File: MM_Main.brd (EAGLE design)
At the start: 74 x 87.2 mm, 81 parts, among them IC1 ULN2003AD, IC2 TB6612FNG, IC4 LD117ADT50TR, IC5 MCP1825, Q1 TEFT4300, Q2 TEFT4300, Q3 TEFT4300, Q4 TEFT4300, Q5 TEFT4300, Q6 TEFT4300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

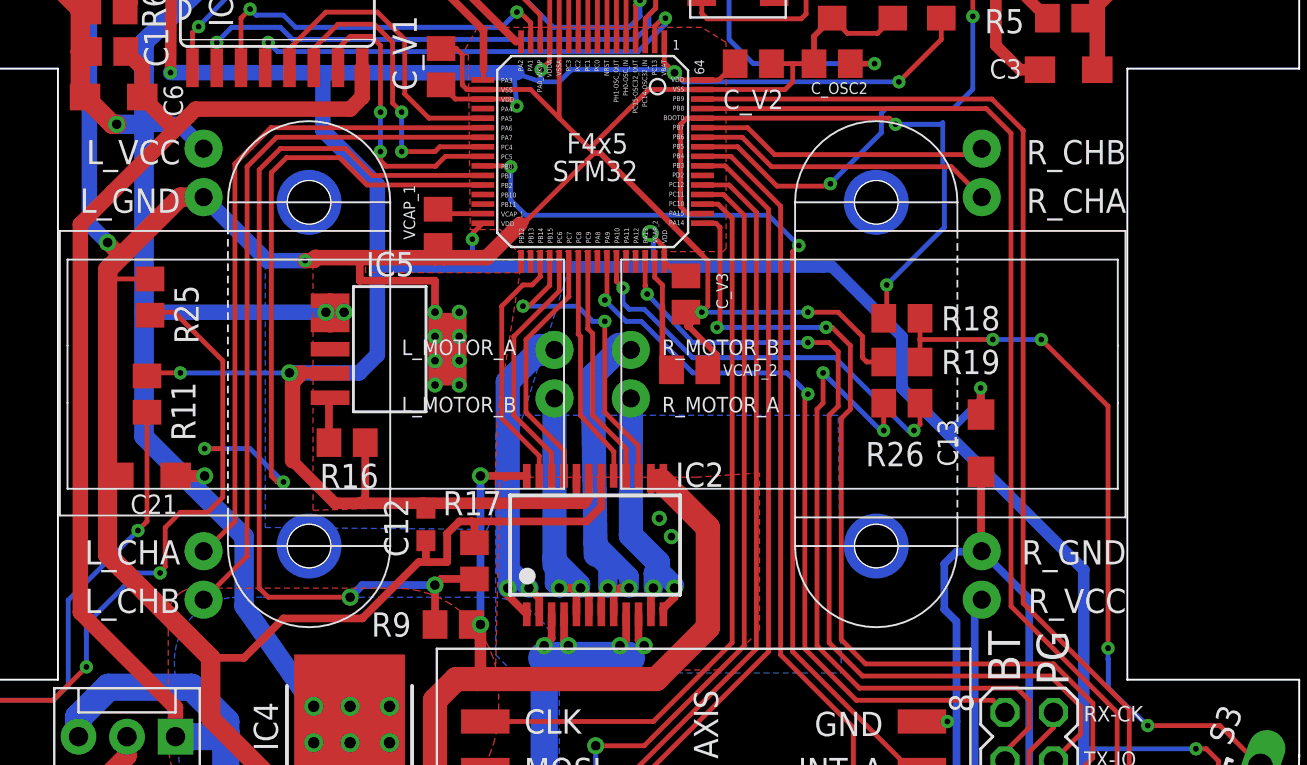
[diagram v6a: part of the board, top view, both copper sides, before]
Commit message: wywalilem elementy ktore byly pod podstawka silnika
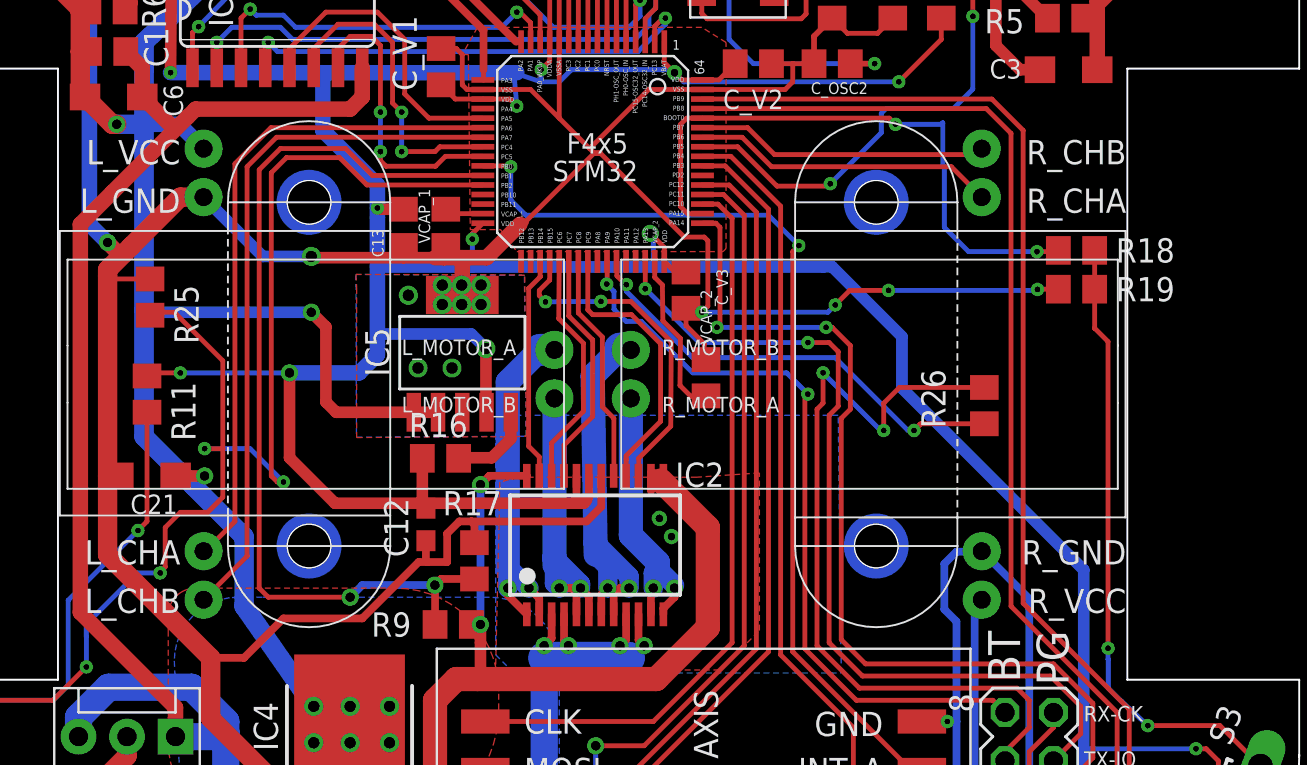
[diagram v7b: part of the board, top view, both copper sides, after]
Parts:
- C13: value tant-a-10u -> 10u; device rcl:SMC_A -> rcl:C0805
- moved C13 32.3 mm to (-9.91, 7.62)
- moved R19 9.91 mm to (25.3, 4.38)
- moved R18 9.81 mm to (25.3, 6.41)
- moved R16 4.96 mm to (-7.97, -4.48), turned to 180 degrees
- moved R26 4.32 mm to (20.5, -1.71), turned to 270 degrees
- moved IC5 3.46 mm to (-6.92, 1.30), turned to 0 degrees
- moved VCAP_2 0.95 mm to (5.94, -0.25), turned to 90 degrees
- moved VCAP_1 0.41 mm to (-7.69, 7.62)
- moved C_V3 0.20 mm to (4.89, 4.33)
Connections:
- net +3V3: now also C13.1; no longer C13.+
- net GND: now also C13.2; no longer C13.-
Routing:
- net +5V: track 298.1 -> 305.8 mm, vias 16 -> 15
- net GND: track 466.4 -> 459.1 mm, vias 20 -> 23
- net N$26: track 36.3 -> 41.9 mm
- net N$23: track 38.0 -> 32.8 mm, vias 4 -> 2
- net +3V3: track 351.2 -> 355.7 mm, vias 14 -> 15
- net MR_IN2: track 12.1 -> 14.7 mm
- net VCAP_2: track 6.32 -> 8.65 mm
- net BT_TXD: track 21.9 -> 24.2 mm
- net N$1: track 2.38 -> 4.54 mm
- net ML_PWM: track 13.2 -> 11.7 mm
- net MR_PWM: track 16.6 -> 17.7 mm
- net ML_IN2: track 13.0 -> 12.4 mm
- net ML_IN1: track 13.0 -> 12.5 mm

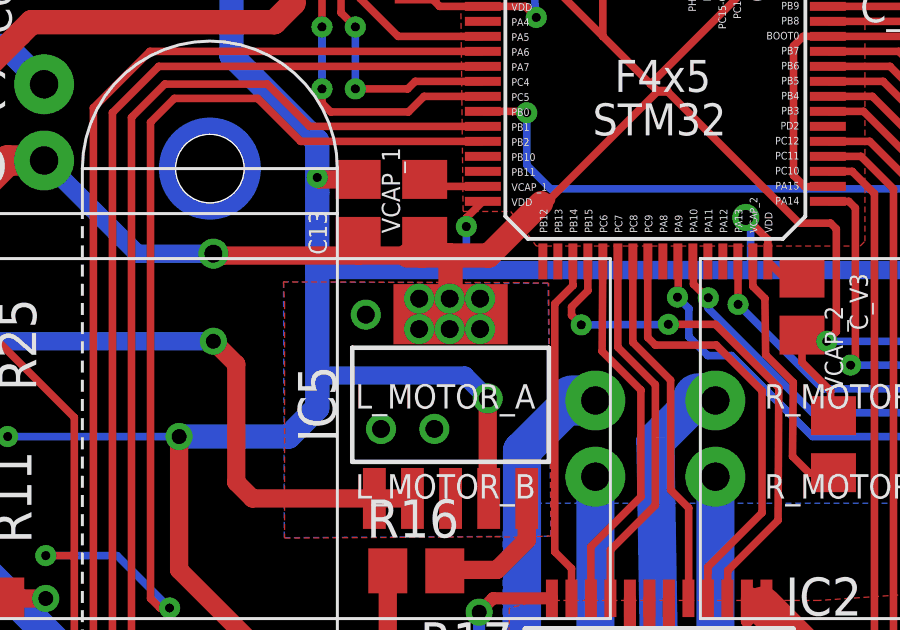
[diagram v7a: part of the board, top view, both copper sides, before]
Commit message: poprawione piny w cubemx
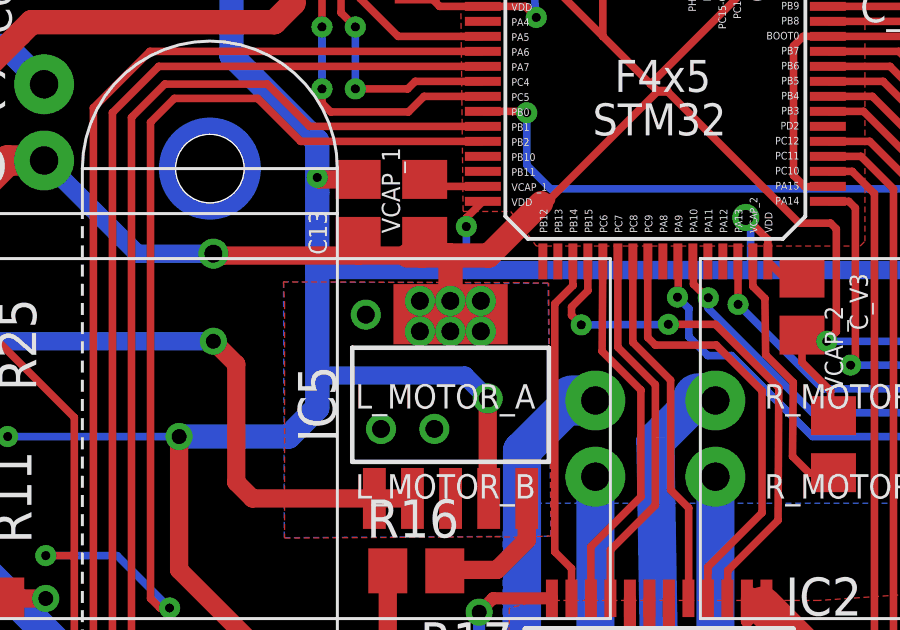
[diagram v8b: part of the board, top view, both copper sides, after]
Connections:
- net ADC_PA3 renamed ADC_LS
- net N$13 renamed SENSOR_LS
- net N$14 renamed SENSOR_RS
- net N$15 renamed SENSOR_R
- net N$16 renamed SENSOR_RF
- net N$2 renamed SENSOR_LF
- net N$33 renamed SENSOR_L
- removed net ADC_PA2: Q2.E, R23.2, U$6.PA2
- new net ADC_RS: Q6.E, R1.2, U$6.PC0
- net ADC_L: now also Q3.E, R4.2, U$6.PC3; no longer Q5.E, R2.2, U$6.PC1
- net ADC_LF: now also Q2.E, R23.2, U$6.PA2; no longer Q6.E, R1.2, U$6.PC0
- net ADC_RF: now also Q5.E, R2.2, U$6.PC1; no longer Q3.E, R4.2, U$6.PC3
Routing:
- net ADC_RS: track 0.00 -> 33.9 mm
- net ADC_PA2: track 30.0 -> 0.00 mm
- net ADC_LF: track 33.9 -> 30.0 mm
- net ADC_RF: track 32.9 -> 36.0 mm
- net ADC_L: track 36.0 -> 32.9 mm
